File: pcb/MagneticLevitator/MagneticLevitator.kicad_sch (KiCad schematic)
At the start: 0 parts

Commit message: updates to pcb
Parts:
- added D1: D, Diode_THT:D_DO-41_SOD81_P7.62mm_Horizontal, symbol Device:D
- added J1: ESP32 Left Side Pins, Connector_PinSocket_2.54mm:PinSocket_1x19_P2.54mm_Vertical, symbol Connector:Conn_01x19_Socket
- added J2: ESP32 Right Side Pins, Connector_PinSocket_2.54mm:PinSocket_1x19_P2.54mm_Vertical, symbol Connector:Conn_01x19_Socket
- added J3, J4: Screw_Terminal_01x02, TerminalBlock:TerminalBlock_MaiXu_MX126-5.0-02P_1x02_P5.00mm, symbol Connector:Screw_Terminal_01x02
- added J5: ACS712T Breakout, Connector_PinSocket_2.54mm:PinSocket_1x03_P2.54mm_Vertical, symbol Connector:Conn_01x03_Socket
- added J6: hall effect sensor breakout, Connector_PinSocket_2.54mm:PinSocket_1x03_P2.54mm_Vertical, symbol Connector:Conn_01x03_Socket
- added Q1: Q_NMOS_GDS, Package_TO_SOT_THT:TO-220-3_Vertical, symbol Transistor_FET:Q_NMOS_GDS
- added R1: 10k, Resistor_THT:R_Axial_DIN0207_L6.3mm_D2.5mm_P10.16mm_Horizontal, symbol Device:R
- added R2: 220, Resistor_THT:R_Axial_DIN0207_L6.3mm_D2.5mm_P10.16mm_Horizontal, symbol Device:R
- added R3: 3.3k, Resistor_THT:R_Axial_DIN0207_L6.3mm_D2.5mm_P10.16mm_Horizontal, symbol Device:R
- added R4: 1.8k, Resistor_THT:R_Axial_DIN0207_L6.3mm_D2.5mm_P10.16mm_Horizontal, symbol Device:R
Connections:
- new net: J5.2 (Pin_2), R3.1, R4.2
- new net: Q1.1 (G), R1.1, R2.2
- new net: D1.2 (A), J4.2 (Pin_2), Q1.2 (D)
- new net: D1.1 (K), J4.1 (Pin_1)
- new net +3V3: J1.1 (Pin_1), J6.2 (Pin_2)
- new net +5V: J1.19 (Pin_19), J3.1 (Pin_1), J5.1 (Pin_1)
- new net COIL_CURRENT: J1.6 (Pin_6), R4.1
- new net GND: J1.14 (Pin_14), J2.1 (Pin_1), J3.2 (Pin_2), J5.3 (Pin_3), J6.1 (Pin_1), Q1.3 (S), R1.2, R3.2
- new net HALL_OUT: J2.5 (Pin_5), J6.3 (Pin_3)
- new net PWM_OUT: J1.9 (Pin_9), R2.1

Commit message: more pcb updates
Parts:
- removed D1: D, Diode_THT:D_DO-41_SOD81_P7.62mm_Horizontal, symbol Device:D
- removed J5: ACS712T Breakout, Connector_PinSocket_2.54mm:PinSocket_1x03_P2.54mm_Vertical, symbol Connector:Conn_01x03_Socket
- removed R4: 1.8k, Resistor_THT:R_Axial_DIN0207_L6.3mm_D2.5mm_P10.16mm_Horizontal, symbol Device:R
- added C1: 100uF, Capacitor_THT:CP_Radial_D6.3mm_P2.50mm, symbol Device:C
- added C2: 10uF, Capacitor_THT:CP_Radial_D6.3mm_P2.50mm, symbol Device:C
- added C3: 100nF, Capacitor_THT:C_Disc_D3.0mm_W1.6mm_P2.50mm, symbol Device:C
- added D2: D_Schottky, Diode_THT:D_DO-201AD_P15.24mm_Horizontal, symbol Device:D_Schottky
- added U1: LM7805_TO220, Package_TO_SOT_THT:TO-220-3_Vertical, symbol Regulator_Linear:LM7805_TO220
- R3: value 3.3k -> 0.1R; footprint Resistor_THT:R_Axial_DIN0207_L6.3mm_D2.5mm_P10.16mm_Horizontal -> Resistor_THT:R_Axial_Power_L25.0mm_W9.0mm_P27.94mm
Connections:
- net COIL_CURRENT is gone; now on net I_COIL: J1.6 (Pin_6)
- net +5V: now also C2.1, C3.1, U1.3 (VO); no longer J3.1 (Pin_1)
- net GND: now also C1.2, C2.2, C3.2, U1.2 (GND); no longer Q1.3 (S)
- net I_COIL: now reaches R3.1
- net I_COIL: now also Q1.3 (S)
- net at J4.2 (Pin_2), Q1.2 (D): now also D2.2 (A)
- net at J4.1 (Pin_1): now also D2.1 (K)
- new net +12V: C1.1, J3.1 (Pin_1), U1.1 (VI)
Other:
- moved on the sheet: J6

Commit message: more PCB updates
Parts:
- added C4: 100nF, Capacitor_THT:C_Disc_D3.0mm_W1.6mm_P2.50mm, symbol Device:C
- added R4, R5: 1k, Resistor_THT:R_Axial_DIN0207_L6.3mm_D2.5mm_P10.16mm_Horizontal, symbol Device:R
- added R6: 15k, Resistor_THT:R_Axial_DIN0207_L6.3mm_D2.5mm_P10.16mm_Horizontal, symbol Device:R
- added U2: MCP6002-xMC, Package_DIP:DIP-8_W7.62mm, symbol Amplifier_Operational:MCP6002-xMC
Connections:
- net +12V: now also D2.1 (K), J4.1 (Pin_1)
- net +3V3: now also U2.8 (V+)
- net GND: now also J2.7 (Pin_7), C4.1, R5.1, U2.4 (V-), U2.5 (+), U2.9 (V-)
- net HALL_OUT: now also J1.4 (Pin_4); no longer J2.5 (Pin_5)
- net I_COIL: now also J1.3 (Pin_3), R6.1, U2.1; no longer J1.6 (Pin_6), Q1.3 (S), R3.1
- new net: R5.2, R6.2, U2.2 (-)
- new net: C4.2, R4.2, U2.3 (+)
- new net: U2.6 (-), U2.7
- new net: Q1.3 (S), R3.1, R4.1
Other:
- moved on the sheet: C1, C2, C3, D2, J1, J2, J3, J4, J6, Q1, R1, R2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

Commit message: more pcb updates
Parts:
- removed C1: 100uF, Capacitor_THT:CP_Radial_D6.3mm_P2.50mm, symbol Device:C
- removed C2: 10uF, Capacitor_THT:CP_Radial_D6.3mm_P2.50mm, symbol Device:C
- removed C3: 100nF, Capacitor_THT:C_Disc_D3.0mm_W1.6mm_P2.50mm, symbol Device:C
- removed J3: Screw_Terminal_01x02, TerminalBlock:TerminalBlock_MaiXu_MX126-5.0-02P_1x02_P5.00mm, symbol Connector:Screw_Terminal_01x02
- removed U1: LM7805_TO220, Package_TO_SOT_THT:TO-220-3_Vertical, symbol Regulator_Linear:LM7805_TO220
- removed U2: MCP6002-xMC, Package_DIP:DIP-8_W7.62mm, symbol Amplifier_Operational:MCP6002-xMC
- added J5: Screw_Terminal_01x03, TerminalBlock:TerminalBlock_MaiXu_MX126-5.0-03P_1x03_P5.00mm, symbol Connector:Screw_Terminal_01x03
- added U1: MCP6002-xP, Package_DIP:DIP-8_W7.62mm, symbol Amplifier_Operational:MCP6002-xP
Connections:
- net +12V: now also J5.1 (Pin_1)
- net +3V3: now also U1.8 (V+)
- net +5V: now also J5.2 (Pin_2)
- net GND: now also J5.3 (Pin_3), U1.4 (V-), U1.5 (+)
- net I_COIL: now also U1.1
- net at R5.2, R6.2: now also U1.2 (-)
- net at C4.2, R4.2: now also U1.3 (+)
- new net: U1.6 (-), U1.7
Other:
- moved on the sheet: C4, D2, J1, J2, J4, J6, Q1, R1, R2, R3, R4, R5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

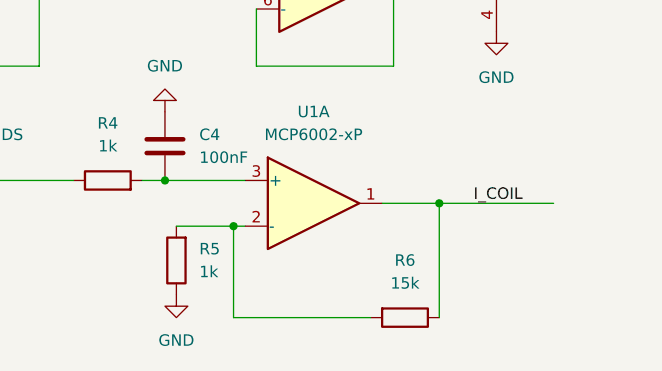
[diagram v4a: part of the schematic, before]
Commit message: added sensor and actuator sections to report
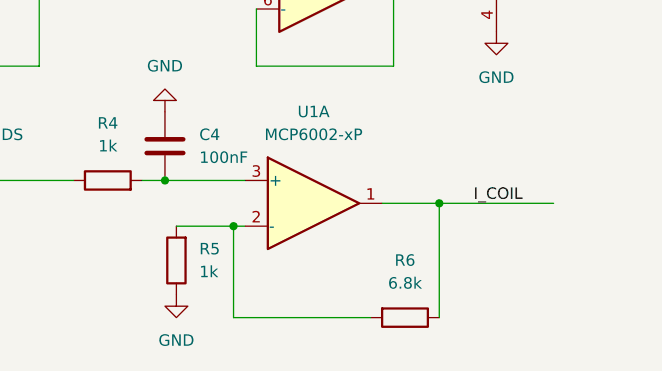
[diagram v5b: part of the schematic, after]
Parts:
- R6: value 15k -> 6.8k
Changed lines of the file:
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@@
 			)
 		)
-		(property "Value" "15k"
+		(property "Value" "6.8k"
 			(at 184.15 127 90)
 			(show_name no)

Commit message: more pcb updates
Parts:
- removed U1: MCP6002-xP, Package_DIP:DIP-8_W7.62mm, symbol Amplifier_Operational:MCP6002-xP
- added U2: LM324N, Package_DIP:DIP-14_W7.62mm, symbol dk_Linear-Amplifiers-Instrumentation-OP-Amps-Buffer-Amps:LM324N
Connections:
- net +5V: now also U2.4 (VCC)
- net GND: now also U2.11 (GND)
- net I_COIL: now also U2.1
- net at R5.2, R6.2: now also U2.3
- net at C4.2, R4.2: now also U2.2

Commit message: cooked
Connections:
- net +3V3: now also J6.1 (Pin_1); no longer J6.2 (Pin_2)
- net GND: now also J6.2 (Pin_2); no longer J6.1 (Pin_1)
- net at R5.2, R6.2: now also U2.2; no longer U2.3
- net at C4.2, R4.2: now also U2.3; no longer U2.2
- net V_HALL: now reaches J1.5 (Pin_5)
- net V_HALL: now also J6.3 (Pin_3)
- net V_SHUNT: now reaches J1.6 (Pin_6)
- net V_SHUNT: now also R6.1, U2.1
- net HALL_OUT: no longer names the net of J1.4 (Pin_4)
- net HALL_OUT: no longer J6.3 (Pin_3)
- removed net I_COIL: J1.3 (Pin_3), R6.1, U2.1
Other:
- moved on the sheet: R5, R6, U2A
